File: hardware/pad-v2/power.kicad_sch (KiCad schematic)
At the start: 43 parts, among them J101 Pogo cable (to floor board), J102 Battery 1x 21700 + NTC, Q101 FS8205A, U101 TPD4E1U06DBVR, U102 WS3222D, U103 ETA6003, U104 DW01A, U105 TLV75733PDBV

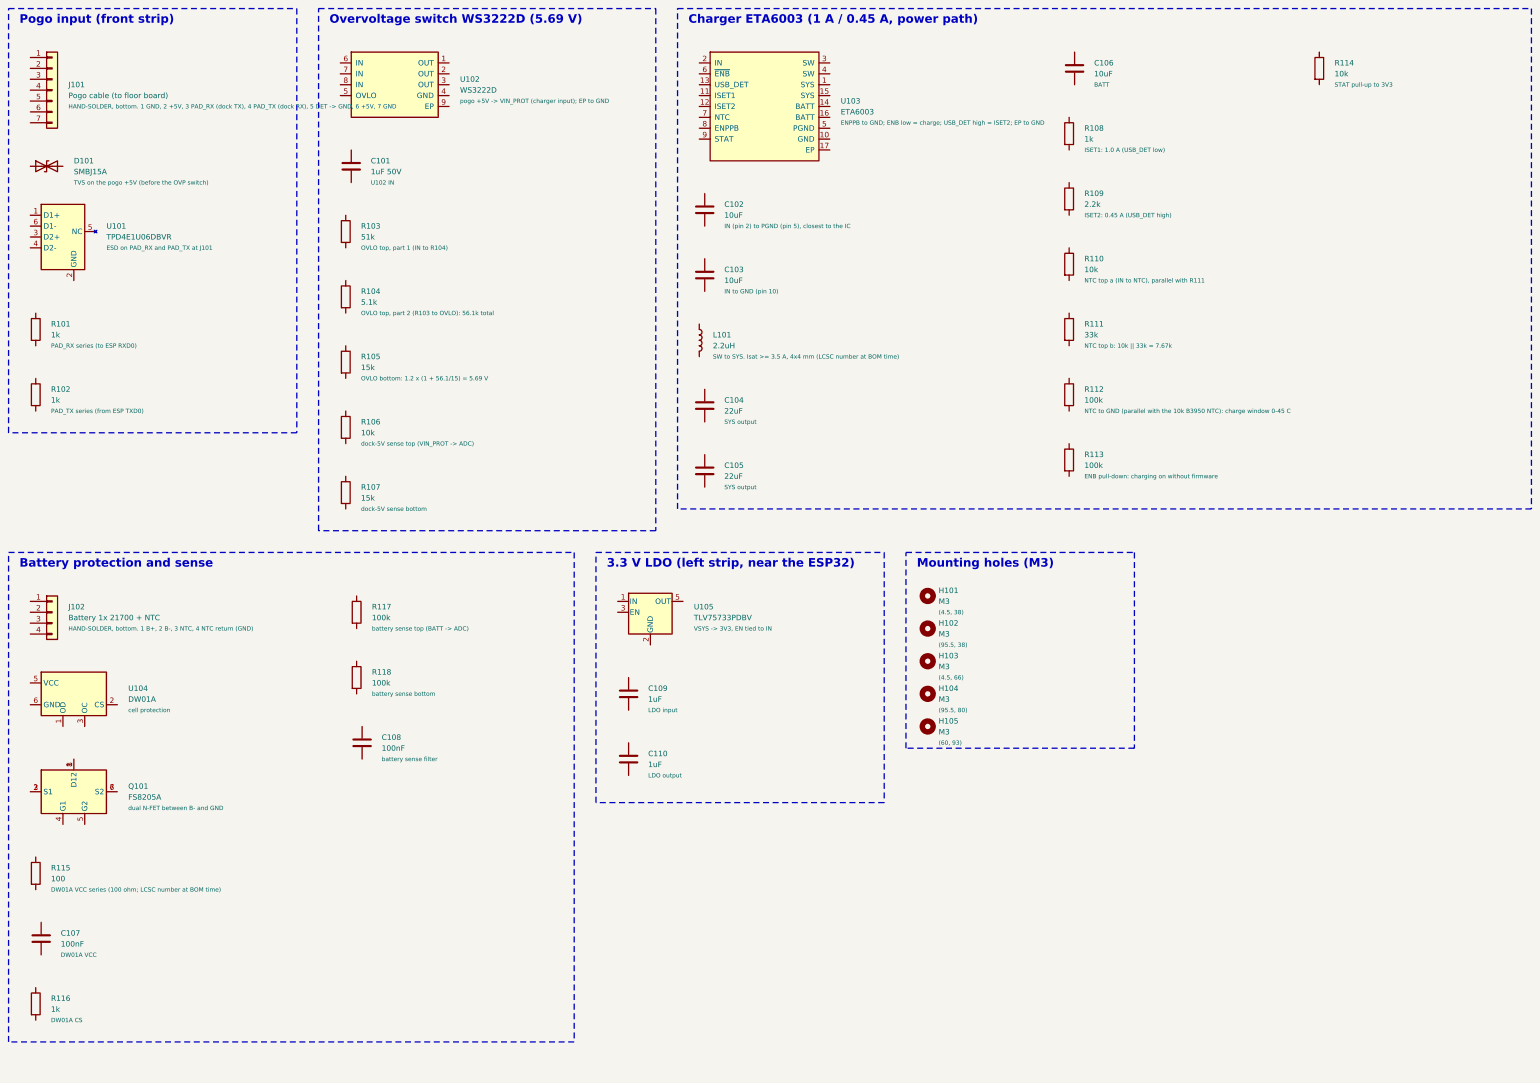
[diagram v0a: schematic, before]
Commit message: Pad v2: GPIO map for routing, PAD_WIRING.md (component-by-component), connection model + checker; battery 2-pin + NTC header, USB-C to the front edge, LED chain starts at key 9
Co-Authored-By: Claude Opus 5.5 <noreply@anthropic.com>
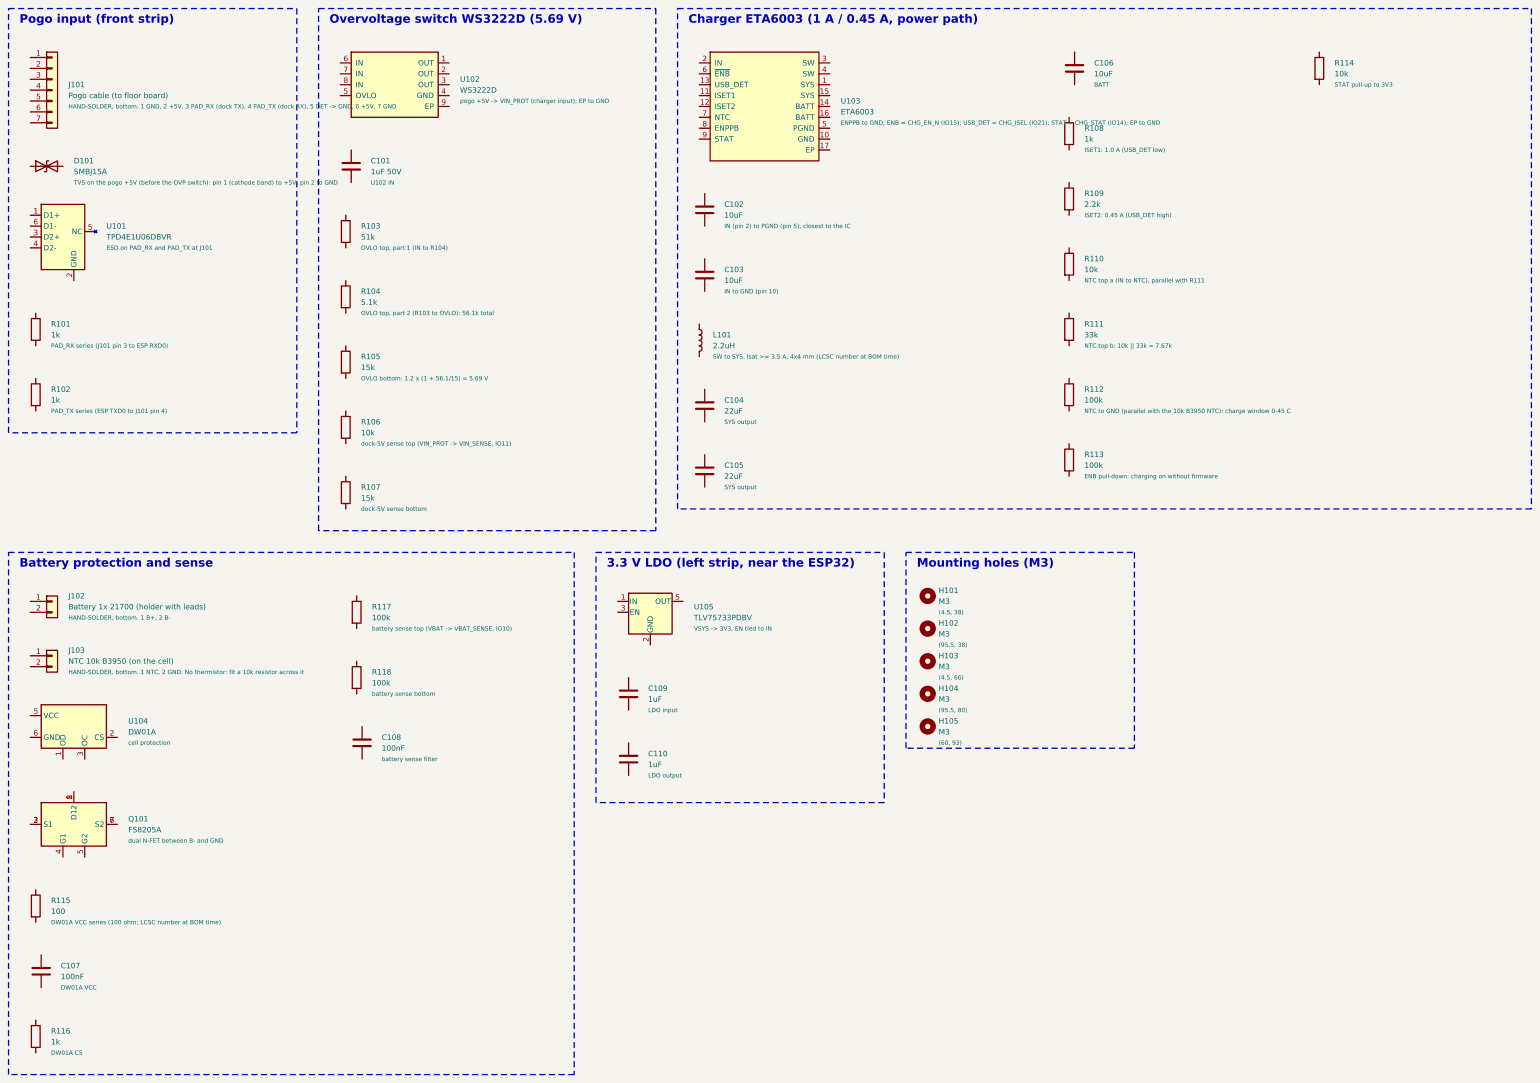
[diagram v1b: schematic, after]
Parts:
- removed J102: Battery 1x 21700 + NTC, Connector_JST:JST_XH_S4B-XH-A_1x04_P2.50mm_Horizontal, symbol Connector_Generic:Conn_01x04
- added J102: Battery 1x 21700 (holder with leads), Connector_JST:JST_XH_S2B-XH-A_1x02_P2.50mm_Horizontal, symbol Connector_Generic:Conn_01x02
- added J103: NTC 10k B3950 (on the cell), Connector_JST:JST_XH_S2B-XH-A_1x02_P2.50mm_Horizontal, symbol Connector_Generic:Conn_01x02
- D101: Note TVS on the pogo +5V (before the OVP switch) -> TVS on the pogo +5V (before the OVP switch): pin 1 (cathode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
- R101: Note PAD_RX series (to ESP RXD0) -> PAD_RX series (J101 pin 3 to ESP RXD0)
- R102: Note PAD_TX series (from ESP TXD0) -> PAD_TX series (ESP TXD0 to J101 pin 4)
- R106: Note dock-5V sense top (VIN_PROT -> ADC) -> dock-5V sense top (VIN_PROT -> VIN_SENSE, IO11)
- R117: Note battery sense top (BATT -> ADC) -> battery sense top (VBAT -> VBAT_SENSE, IO10)
- U103: Note ENPPB to GND; ENB low = charge; USB_DET high = ISET2; EP to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 -> ENPPB to GND; ENB = CHG_EN_N (IO15); USB_DET = CHG_ISEL (IO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
